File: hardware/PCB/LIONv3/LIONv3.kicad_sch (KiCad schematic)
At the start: 41 parts, among them SW1 RESET, SW2 BOOT, U1 TCAN3414DR, U14 UART, U15 I2C, U16 CAN, U17 PWR_3V3, U18 PWR_5V, U19 PWR_GND, U2 TYPE-C_16PIN_2MD(073), U3 ESP32-C6-MINI-1-N4, U4 TMP112AIDRLR

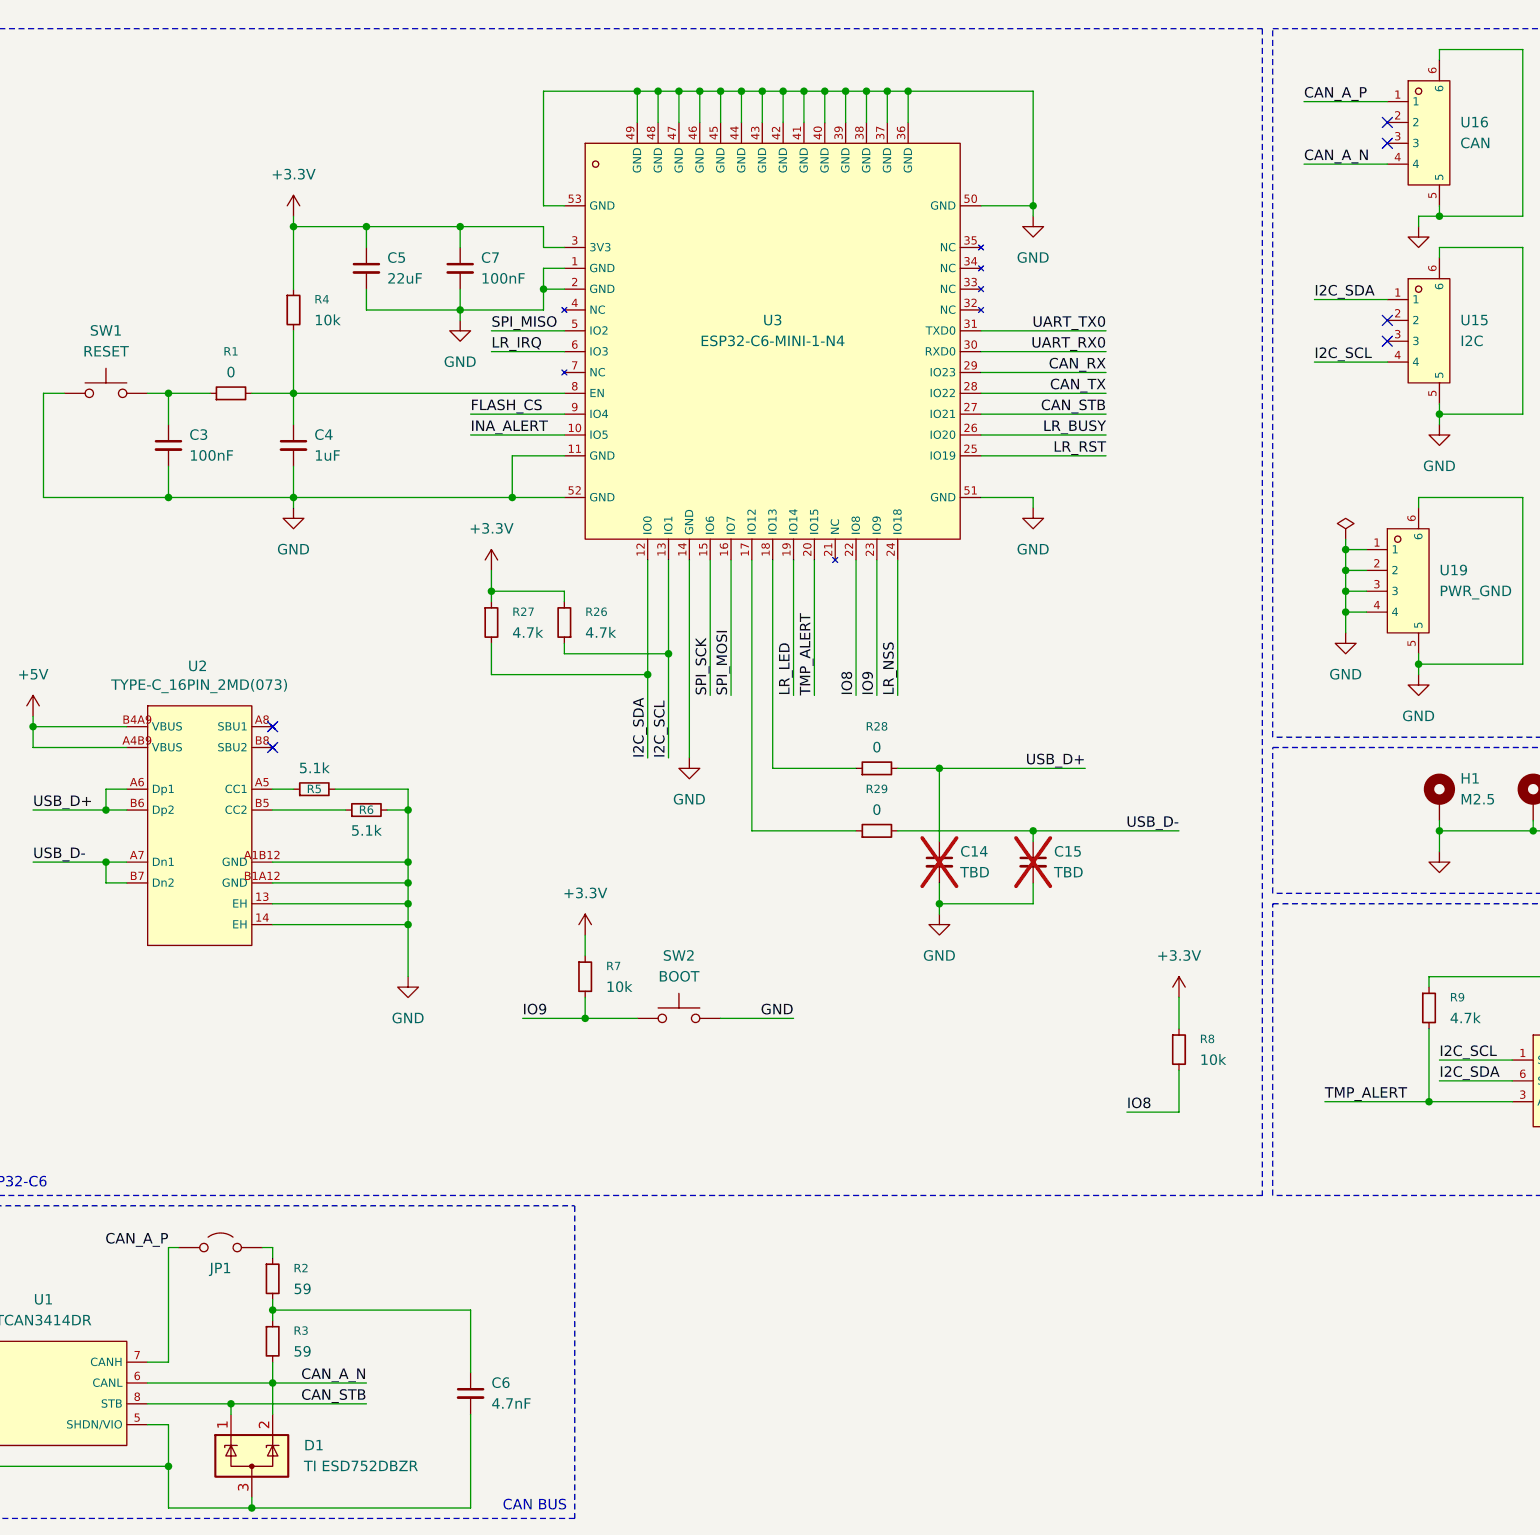
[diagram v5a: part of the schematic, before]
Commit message: feat(hardware): PCB macro placement
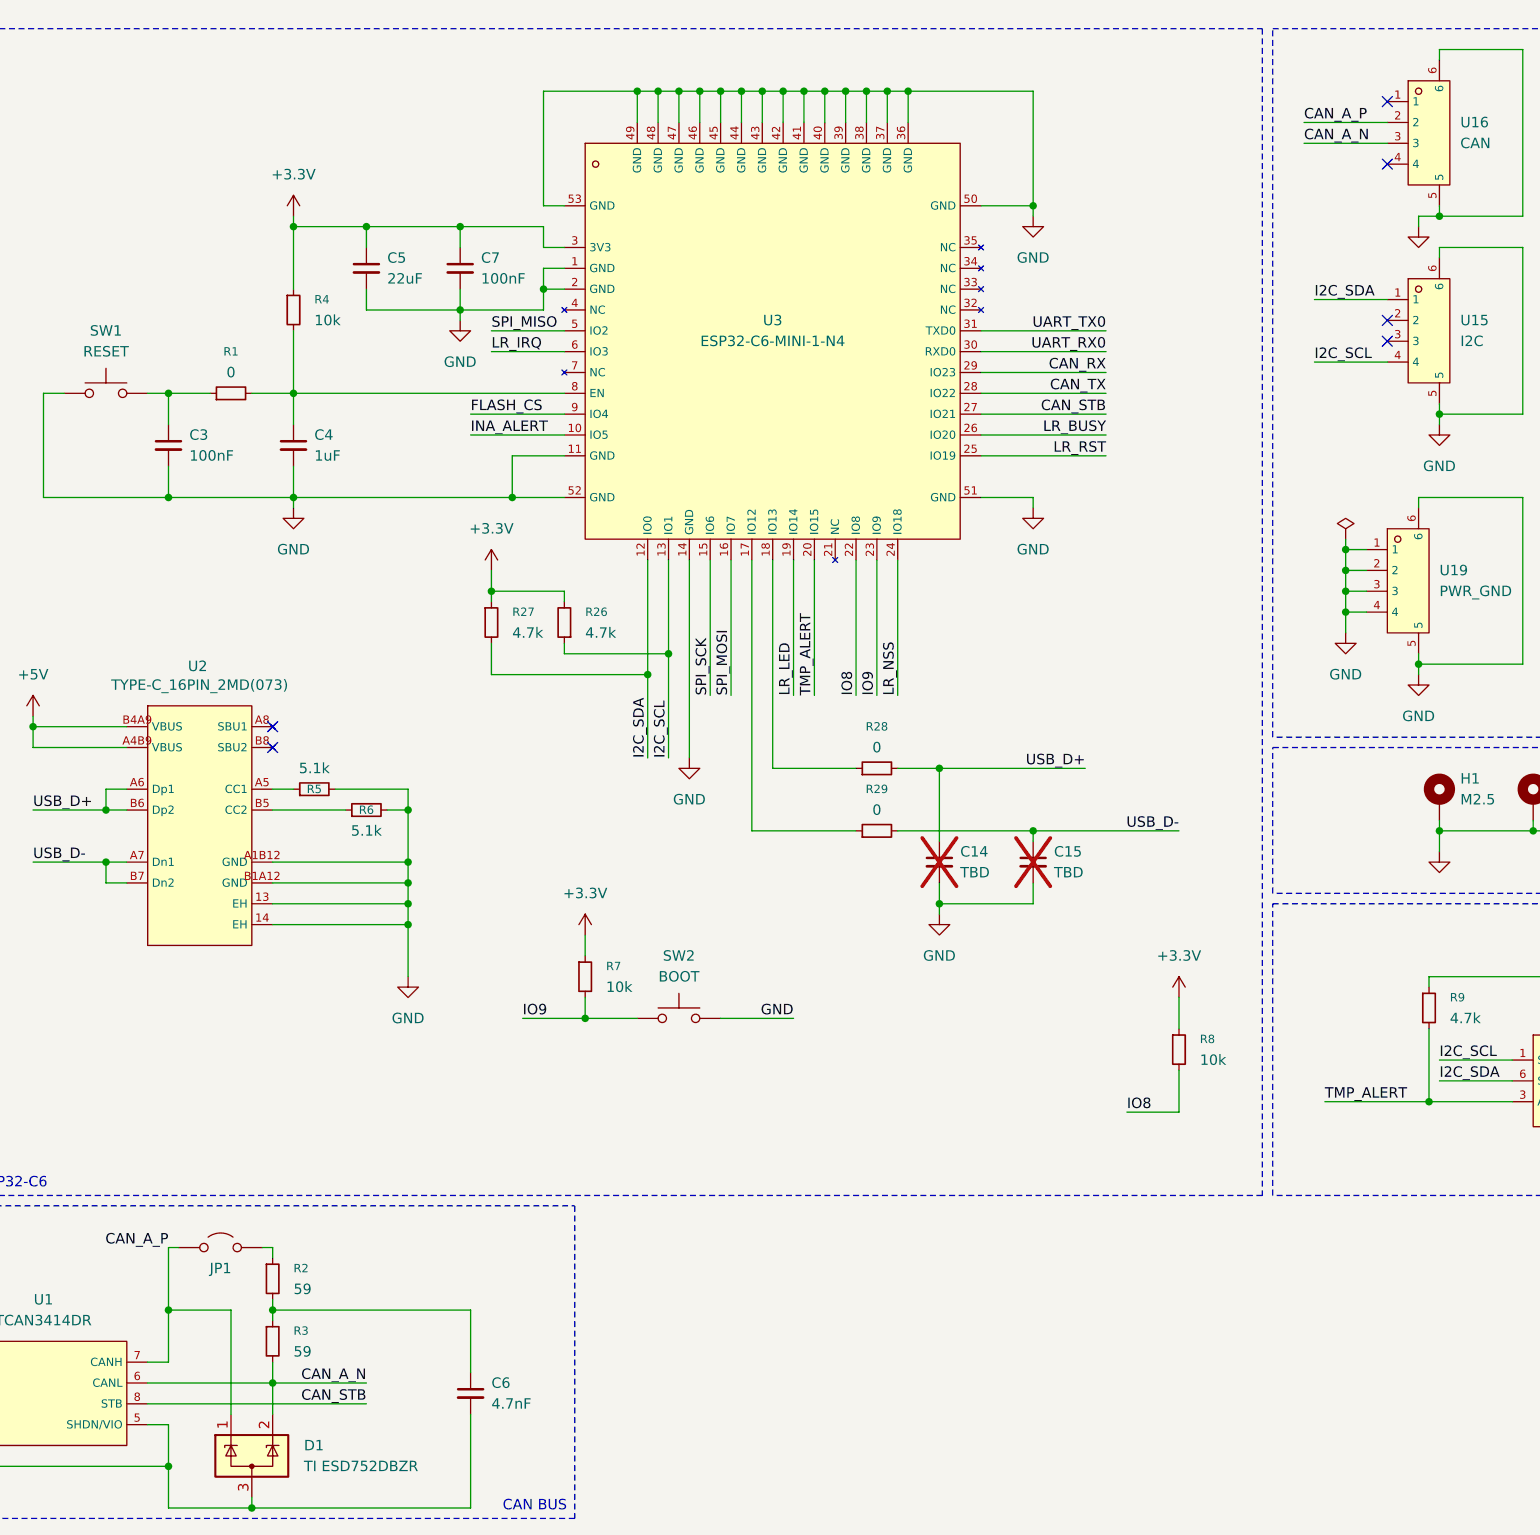
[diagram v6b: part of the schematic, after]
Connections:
- net CAN_A_N: now also U16.3; no longer U16.4
- net CAN_A_P: now also D1.1 (K), U16.2; no longer U16.1
- net CAN_STB: no longer D1.1 (K)
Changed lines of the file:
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@@
 	)
 	(junction
-		(at 81.28 181.61)
-		(diameter 0)
-		(color 0 0 0 0)
-	)
-	(junction
 		(at 138.43 21.59)
 		(diameter 0)
@@
 	)
 	(junction
+		(at 73.66 170.18)
+		(diameter 0)
+		(color 0 0 0 0)
+	)
+	(junction
 		(at 247.65 80.01)
 		(diameter 0)
@@
 	)
 	(no_connect
-		(at 222.25 25.4)
+		(at 222.25 30.48)
 	)
 	(no_connect
@@
 	)
 	(no_connect
-		(at 222.25 27.94)
+		(at 222.25 49.53)
 	)
 	(no_connect
-		(at 222.25 49.53)
+		(at 222.25 22.86)
 	)
 	(wire
@@
 	(wire
 		(pts
-			(xy 212.09 30.48) (xy 222.25 30.48)
-		)
-		(stroke
-			(width 0)
-			(type default)
-		)
-	)
-	(wire
-		(pts
 			(xy 153.67 21.59) (xy 153.67 25.4)
 		)
@@
 	(wire
 		(pts
-			(xy 81.28 181.61) (xy 81.28 182.88)
-		)
-		(stroke
-			(width 0)
-			(type default)
-		)
-	)
-	(wire
-		(pts
 			(xy 35.56 181.61) (xy 45.72 181.61)
 		)
@@
 	(wire
 		(pts
+			(xy 73.66 170.18) (xy 73.66 162.56)
+		)
+		(stroke
+			(width 0)
+			(type default)
+		)
+	)
+	(wire
+		(pts
 			(xy 172.72 60.96) (xy 187.96 60.96)
 		)
@@
 	(wire
 		(pts
+			(xy 212.09 25.4) (xy 222.25 25.4)
+		)
+		(stroke
+			(width 0)
+			(type default)
+		)
+	)
+	(wire
+		(pts
 			(xy 172.72 50.8) (xy 187.96 50.8)
 		)
@@
 	(wire
 		(pts
-			(xy 73.66 176.53) (xy 73.66 162.56)
+			(xy 73.66 176.53) (xy 73.66 170.18)
 		)
 		(stroke
@@
 	(wire
 		(pts
-			(xy 81.28 181.61) (xy 97.79 181.61)
-		)
-		(stroke
-			(width 0)
-			(type default)
-		)
-	)
-	(wire
-		(pts
 			(xy 119.38 48.26) (xy 109.22 48.26)
 		)
@@
 	(wire
 		(pts
-			(xy 212.09 22.86) (xy 222.25 22.86)
+			(xy 88.9 62.23) (xy 88.9 58.42)
 		)
 		(stroke
@@
 	(wire
 		(pts
-			(xy 88.9 62.23) (xy 88.9 58.42)
+			(xy 135.89 21.59) (xy 135.89 25.4)
 		)
 		(stroke
@@
 	(wire
 		(pts
-			(xy 135.89 21.59) (xy 135.89 25.4)
+			(xy 30.48 46.99) (xy 48.26 46.99)
 		)
 		(stroke
@@
 	(wire
 		(pts
-			(xy 30.48 46.99) (xy 48.26 46.99)
+			(xy 81.28 170.18) (xy 73.66 170.18)
 		)
 		(stroke
@@
 	(wire
 		(pts
-			(xy 71.12 181.61) (xy 81.28 181.61)
+			(xy 71.12 181.61) (xy 97.79 181.61)
 		)
 		(stroke
@@
 	(wire
 		(pts
+			(xy 212.09 27.94) (xy 222.25 27.94)
+		)
+		(stroke
+			(width 0)
+			(type default)
+		)
+	)
+	(wire
+		(pts
 			(xy 265.43 142.24) (xy 265.43 144.78)
 		)
@@
 	(wire
 		(pts
+			(xy 81.28 182.88) (xy 81.28 170.18)
+		)
+		(stroke
+			(width 0)
+			(type default)
+		)
+	)
+	(wire
+		(pts
 			(xy 247.65 77.47) (xy 251.46 77.47)
 		)
@@
 	)
 	(label "CAN_A_N"
-		(at 212.09 30.48 0)
+		(at 212.09 27.94 0)
 		(effects
 			(font
@@
 	)
 	(label "CAN_A_P"
-		(at 212.09 22.86 0)
+		(at 212.09 25.4 0)
 		(effects
 			(font
